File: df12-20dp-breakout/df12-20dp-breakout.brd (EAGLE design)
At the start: 27.6 x 19 mm, 3 parts, among them J1 DF12(4.0)-20DP-0.5V(86)

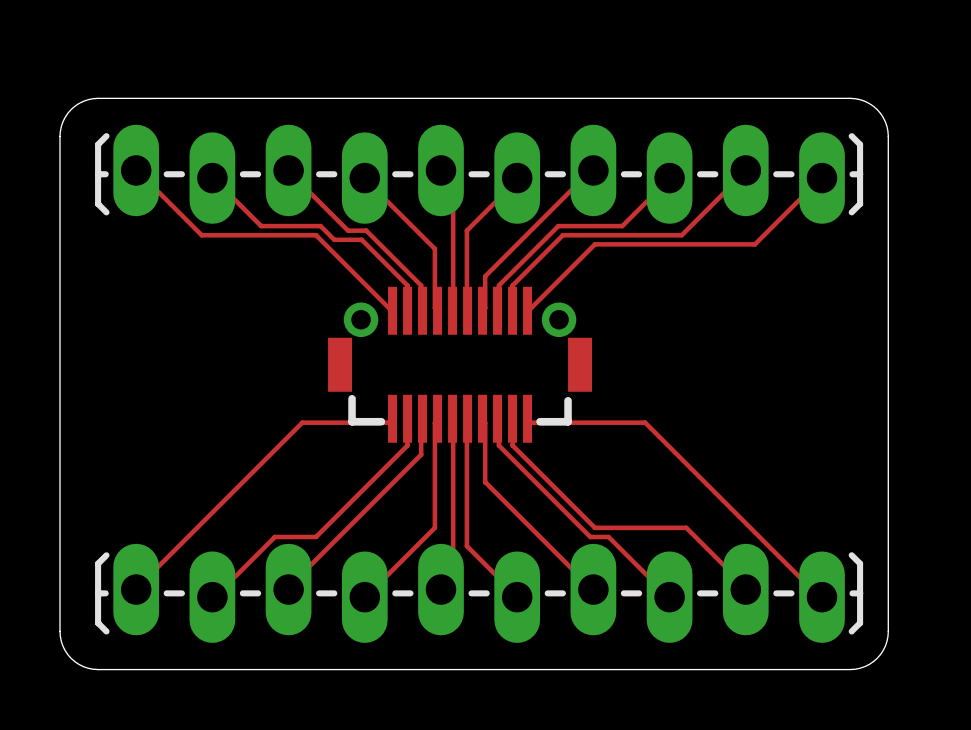
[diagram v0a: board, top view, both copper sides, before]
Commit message: Align pins to multiple of .1 for breadboard
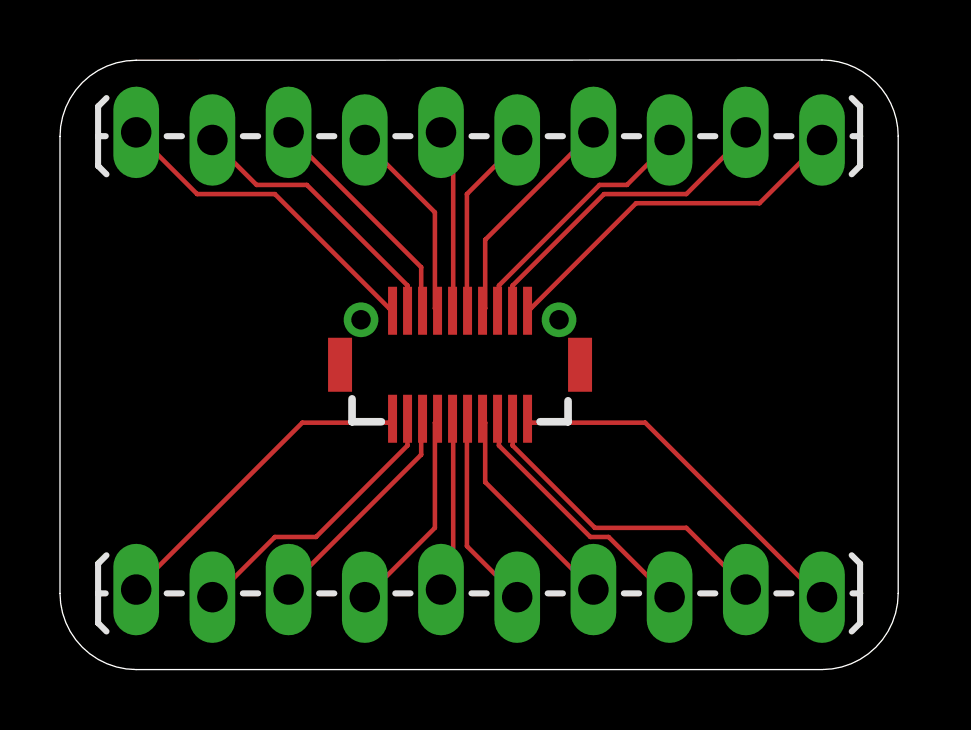
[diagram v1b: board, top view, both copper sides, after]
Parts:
- moved J3 1.27 mm to (2.54, 17.8)
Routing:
- net N$16: track 5.12 -> 6.39 mm
- net N$14: track 5.42 -> 6.69 mm
- net N$15: track 4.89 -> 6.13 mm
- net N$17: track 6.25 -> 7.49 mm
- net N$13: track 6.88 -> 7.79 mm
- net N$19: track 10.2 -> 10.8 mm
- net N$18: track 8.04 -> 8.59 mm
- net N$20: track 11.6 -> 12.2 mm
- net N$12: track 8.82 -> 9.36 mm
- net N$11: track 10.5 -> 11.0 mm
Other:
- board size 27.6 x 19 mm -> 27.9 x 20.3 mm

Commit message: Add silkscreen
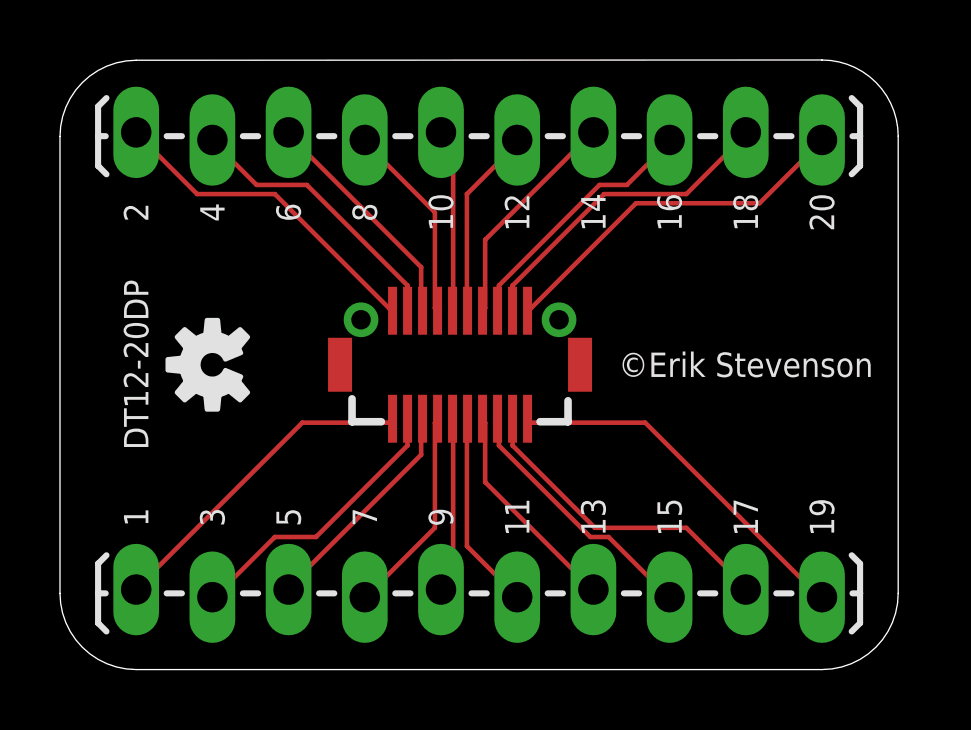
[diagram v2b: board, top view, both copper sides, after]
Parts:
- added U$1: (no value), SparkFun-Aesthetics:OSHW-LOGO-S
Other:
- board text added: "1"
- board text added: "10"
- board text added: "11"
- board text added: "12"
- board text added: "13"
- board text added: "14"
- board text added: "15"
- board text added: "16"
- board text added: "17"
- board text added: "18"
- board text added: "19"
- board text added: "2"
- board text added: "20"
- board text added: "3"
- board text added: "4"
- board text added: "5"
- board text added: "6"
- board text added: "7"
- board text added: "8"
- board text added: "9"
- board text added: "DT12-20DP"
- board text added: "©Erik Stevenson"
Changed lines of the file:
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@@
 <layer number="27" name="tValues" color="7" fill="1" visible="yes" active="yes"/>
 <layer number="28" name="bValues" color="7" fill="1" visible="yes" active="yes"/>
-<layer number="29" name="tStop" color="7" fill="3" visible="no" active="yes"/>
-<layer number="30" name="bStop" color="7" fill="6" visible="no" active="yes"/>
-<layer number="31" name="tCream" color="7" fill="4" visible="no" active="yes"/>
-<layer number="32" name="bCream" color="7" fill="5" visible="no" active="yes"/>
-<layer number="33" name="tFinish" color="6" fill="3" visible="no" active="yes"/>
-<layer number="34" name="bFinish" color="6" fill="6" visible="no" active="yes"/>
-<layer number="35" name="tGlue" color="7" fill="4" visible="no" active="yes"/>
-<layer number="36" name="bGlue" color="7" fill="5" visible="no" active="yes"/>
-<layer number="37" name="tTest" color="7" fill="1" visible="no" active="yes"/>
-<layer number="38" name="bTest" color="7" fill="1" visible="no" active="yes"/>
-<layer number="39" name="tKeepout" color="4" fill="11" visible="no" active="yes"/>
-<layer number="40" name="bKeepout" color="1" fill="11" visible="no" active="yes"/>
-<layer number="41" name="tRestrict" color="4" fill="10" visible="no" active="yes"/>
-<layer number="42" name="bRestrict" color="1" fill="10" visible="no" active="yes"/>
-<layer number="43" name="vRestrict" color="2" fill="10" visible="no" active="yes"/>
-<layer number="44" name="Drills" color="7" fill="1" visible="no" active="yes"/>
-<layer number="45" name="Holes" color="7" fill="1" visible="no" active="yes"/>
-<layer number="46" name="Milling" color="3" fill="1" visible="no" active="yes"/>
-<layer number="47" name="Measures" color="7" fill="1" visible="no" active="yes"/>
+<layer number="29" name="tStop" color="7" fill="3" visible="yes" active="yes"/>
+<layer number="30" name="bStop" color="7" fill="6" visible="yes" active="yes"/>
+<layer number="31" name="tCream" color="7" fill="4" visible="yes" active="yes"/>
+<layer number="32" name="bCream" color="7" fill="5" visible="yes" active="yes"/>
+<layer number="33" name="tFinish" color="6" fill="3" visible="yes" active="yes"/>
+<layer number="34" name="bFinish" color="6" fill="6" visible="yes" active="yes"/>
+<layer number="35" name="tGlue" color="7" fill="4" visible="yes" active="yes"/>
+<layer number="36" name="bGlue" color="7" fill="5" visible="yes" active="yes"/>
+<layer number="37" name="tTest" color="7" fill="1" visible="yes" active="yes"/>
+<layer number="38" name="bTest" color="7" fill="1" visible="yes" active="yes"/>
+<layer number="39" name="tKeepout" color="4" fill="11" visible="yes" active="yes"/>
+<layer number="40" name="bKeepout" color="1" fill="11" visible="yes" active="yes"/>
+<layer number="41" name="tRestrict" color="4" fill="10" visible="yes" active="yes"/>
+<layer number="42" name="bRestrict" color="1" fill="10" visible="yes" active="yes"/>
+<layer number="43" name="vRestrict" color="2" fill="10" visible="yes" active="yes"/>
+<layer number="44" name="Drills" color="7" fill="1" visible="yes" active="yes"/>
+<layer number="45" name="Holes" color="7" fill="1" visible="yes" active="yes"/>
+<layer number="46" name="Milling" color="3" fill="1" visible="yes" active="yes"/>
+<layer number="47" name="Measures" color="7" fill="1" visible="yes" active="yes"/>
 <layer number="48" name="Document" color="7" fill="1" visible="yes" active="yes"/>
 <layer number="49" name="Reference" color="7" fill="1" visible="yes" active="yes"/>
@@
 <wire x1="25.399046875" y1="20.319046875" x2="2.539046875" y2="20.310478125" width="0" layer="20"/>
 <wire x1="2.539046875" y1="20.310478125" x2="0" y2="17.770478125" width="0" layer="20" curve="89.934741"/>
+<text x="2.54" y="5.08" size="0.8128" layer="21" font="vector" ratio="18" rot="R90" align="center">1</text>
+<text x="2.54" y="15.24" size="0.8128" layer="21" font="vector" ratio="18" rot="R90" align="center">2</text>
+<text x="5.08" y="15.24" size="0.8128" layer="21" font="vector" ratio="18" rot="R90" align="center">4</text>
+<text x="7.62" y="15.24" size="0.8128" layer="21" font="vector" ratio="18" rot="R90" align="center">6</text>
+<text x="10.16" y="15.24" size="0.8128" layer="21" font="vector" ratio="18" rot="R90" align="center">8</text>
+<text x="12.7" y="15.24" size="0.8128" layer="21" font="vector" ratio="18" rot="R90" align="center">10</text>
+<text x="15.24" y="15.24" size="0.8128" layer="21" font="vector" ratio="18" rot="R90" align="center">12</text>
+<text x="17.78" y="15.24" size="0.8128" layer="21" font="vector" ratio="18" rot="R90" align="center">14</text>
+<text x="20.32" y="15.24" size="0.8128" layer="21" font="vector" ratio="18" rot="R90" align="center">16</text>
+<text x="22.86" y="15.24" size="0.8128" layer="21" font="vector" ratio="18" rot="R90" align="center">18</text>
+<text x="25.4" y="15.24" size="0.8128" layer="21" font="vector" ratio="18" rot="R90" align="center">20</text>
+<text x="5.08" y="5.08" size="0.8128" layer="21" font="vector" ratio="18" rot="R90" align="center">3</text>
+<text x="7.62" y="5.08" size="0.8128" layer="21" font="vector" ratio="18" rot="R90" align="center">5</text>
+<text x="10.16" y="5.08" size="0.8128" layer="21" font="vector" ratio="18" rot="R90" align="center">7</text>
+<text x="12.7" y="5.08" size="0.8128" layer="21" font="vector" ratio="18" rot="R90" align="center">9</text>
+<text x="15.24" y="5.08" size="0.8128" layer="21" font="vector" ratio="18" rot="R90" align="center">11</text>
+<text x="17.78" y="5.08" size="0.8128" layer="21" font="vector" ratio="18" rot="R90" align="center">13</text>
+<text x="20.32" y="5.08" size="0.8128" layer="21" font="vector" ratio="18" rot="R90" align="center">15</text>
+<text x="22.86" y="5.08" size="0.8128" layer="21" font="vector" ratio="18" rot="R90" align="center">17</text>
+<text x="25.4" y="5.08" size="0.8128" layer="21" font="vector" ratio="18" rot="R90" align="center">19</text>
+<text x="2.54" y="10.16" size="0.8128" layer="21" font="vector" ratio="6" rot="R90" align="center">DT12-20DP</text>
+<text x="22.86" y="10.16" size="0.8128" layer="21" font="vector" ratio="6" rot="R180" align="center">©Erik Stevenson</text>
 </plain>
 <attributes>
@@
 <attribute name="VALUE" x="1.27" y="15.367" size="0.6096" layer="27" font="vector" ratio="20"/>
 </element>
+<element name="U$1" library="SparkFun-Aesthetics" package="OSHW-LOGO-S" value="" x="5.08" y="10.16" rot="R90"/>
 </elements>
 <signals>
